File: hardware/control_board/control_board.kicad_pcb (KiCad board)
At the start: 2 copper layers, 80 x 80 mm, 125 parts, among them J1 SWD, J2 Aux, J3 Panel, J4 6.5/2mm, J5 USB_C, J6 RTD, J7 TC, J8 Conn_01x01, J9 Conn_01x01, Q1 2N7002A, Q2 IRF1018ESTRLPBF, SW1 Reset, SW2 Power, U1 STM32F103C8T6, U2 LMR38010SDDAR, U3 TLV76133DCYR, U4 USBLC6-2SC6, U5 MAX6675, U6 MCP6N11T-005E, U7 MCP6001T, U8 TLP183, Y1 8MHz

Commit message: Remove copper fills around mounting holes
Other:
- board text added: "20231127"
- board text added: "Supervisor: A. Bondyra, Ph.D."
- board text removed: "20231114"
- board text removed: "Promoter: A. Bondyra, Ph.D."

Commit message: Change MCU to STM32F103CBT6
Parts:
- U1: value STM32F103C8T6 -> STM32F103CBT6
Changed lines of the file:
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@@
         (effects (font (size 1 1) (thickness 0.15)))
     )
-    (fp_text value "STM32F103C8T6" (at 2.8 4.65) (layer "F.Fab")
+    (fp_text value "STM32F103CBT6" (at 2.8 4.65) (layer "F.Fab")
         (effects (font (size 1 1) (thickness 0.15)))
     )

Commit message: Release v1.1
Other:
- board text added: "20231129"
- board text removed: "20231127"
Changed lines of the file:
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@@
   (title_block
     (title "Reflow Hot Plate Control Board")
-    (date "2023-11-14")
+    (date "2023-11-29")
     (rev "${REVISION}")
     (company "Author: I. Kajdan")
@@
     (fp_line (start 5.625 5) (end 4.625 5)
       (stroke (width 0.1) (type solid)) (layer "F.Fab"))
-    (pad "1" smd roundrect (at -7.65 -2.54 90) (size 4.6 1.1) (layers "F.Cu" "F.Paste" "F.Mask") (roundrect_rratio 0.227273)
+    (pad "1" smd roundrect (at -7.65 -2.54 90) (size 4.6 1.1) (layers "F.Cu" "F.Paste" "F.Mask") (roundrect_rratio 0.2272727273)
       (net 24 "Net-(D9-K)") (pinfunction "G") (pintype "input"))
-    (pad "2" smd roundrect (at -0.925 -2.775 90) (size 4.55 5.25) (layers "F.Cu" "F.Paste") (roundrect_rratio 0.054945)
+    (pad "2" smd roundrect (at -0.925 -2.775 90) (size 4.55 5.25) (layers "F.Cu" "F.Paste") (roundrect_rratio 0.05494505495)
       (net 92 "Net-(D10-A)") (pinfunction "D") (pintype "passive"))
-    (pad "2" smd roundrect (at -0.925 2.775 90) (size 4.55 5.25) (layers "F.Cu" "F.Paste") (roundrect_rratio 0.054945)
+    (pad "2" smd roundrect (at -0.925 2.775 90) (size 4.55 5.25) (layers "F.Cu" "F.Paste") (roundrect_rratio 0.05494505495)
       (net 92 "Net-(D10-A)") (pinfunction "D") (pintype "passive"))
-    (pad "2" smd roundrect (at 1.5 0 90) (size 9.4 10.8) (layers "F.Cu" "F.Mask") (roundrect_rratio 0.026596)
+    (pad "2" smd roundrect (at 1.5 0 90) (size 9.4 10.8) (layers "F.Cu" "F.Mask") (roundrect_rratio 0.02659595745)
       (net 92 "Net-(D10-A)") (pinfunction "D") (pintype "passive"))
-    (pad "2" smd roundrect (at 3.925 -2.775 90) (size 4.55 5.25) (layers "F.Cu" "F.Paste") (roundrect_rratio 0.054945)
+    (pad "2" smd roundrect (at 3.925 -2.775 90) (size 4.55 5.25) (layers "F.Cu" "F.Paste") (roundrect_rratio 0.05494505495)
       (net 92 "Net-(D10-A)") (pinfunction "D") (pintype "passive"))
-    (pad "2" smd roundrect (at 3.925 2.775 90) (size 4.55 5.25) (layers "F.Cu" "F.Paste") (roundrect_rratio 0.054945)
+    (pad "2" smd roundrect (at 3.925 2.775 90) (size 4.55 5.25) (layers "F.Cu" "F.Paste") (roundrect_rratio 0.05494505495)
       (net 92 "Net-(D10-A)") (pinfunction "D") (pintype "passive"))
-    (pad "3" smd roundrect (at -7.65 2.54 90) (size 4.6 1.1) (layers "F.Cu" "F.Paste" "F.Mask") (roundrect_rratio 0.227273)
+    (pad "3" smd roundrect (at -7.65 2.54 90) (size 4.6 1.1) (layers "F.Cu" "F.Paste" "F.Mask") (roundrect_rratio 0.2272727273)
       (net 2 "GND") (pinfunction "S") (pintype "passive"))
     (model "${KICAD6_3DMODEL_DIR}/Package_TO_SOT_SMD.3dshapes/TO-263-2.wrl"
@@
     (fp_line (start 7.45 3.4) (end 7.45 -2.35)
       (stroke (width 0.1) (type solid)) (layer "F.Fab"))
-    (pad "1" thru_hole roundrect (at 0 0 90) (size 1.7 1.95) (drill 0.95) (layers "*.Cu" "*.Mask") (roundrect_rratio 0.147059)
+    (pad "1" thru_hole roundrect (at 0 0 90) (size 1.7 1.95) (drill 0.95) (layers "*.Cu" "*.Mask") (roundrect_rratio 0.1470588235)
       (net 50 "/Temperature Sensors/IN+") (pinfunction "Pin_1") (pintype "passive"))
     (pad "2" thru_hole oval (at 2.5 0 90) (size 1.7 1.95) (drill 0.95) (layers "*.Cu" "*.Mask")
@@
     (fp_line (start 4.95 3.4) (end 4.95 -2.35)
       (stroke (width 0.1) (type solid)) (layer "F.Fab"))
-    (pad "1" thru_hole roundrect (at 0 0 90) (size 1.7 2) (drill 1) (layers "*.Cu" "*.Mask") (roundrect_rratio 0.147059)
+    (pad "1" thru_hole roundrect (at 0 0 90) (size 1.7 2) (drill 1) (layers "*.Cu" "*.Mask") (roundrect_rratio 0.1470588235)
       (net 84 "Net-(J7-Pin_1)") (pinfunction "Pin_1") (pintype "passive"))
     (pad "2" thru_hole oval (at 2.5 0 90) (size 1.7 2) (drill 1) (layers "*.Cu" "*.Mask")
@@
     (fp_line (start 2.25 1.6) (end -2.25 1.6)
       (stroke (width 0.1) (type solid)) (layer "F.Fab"))
-    (pad "1" smd roundrect (at -2.1375 0) (size 1.125 3.4) (layers "F.Cu" "F.Paste" "F.Mask") (roundrect_rratio 0.222222)
+    (pad "1" smd roundrect (at -2.1375 0) (size 1.125 3.4) (layers "F.Cu" "F.Paste" "F.Mask") (roundrect_rratio 0.2222222222)
       (net 23 "+24V") (pintype "passive"))
-    (pad "2" smd roundrect (at 2.1375 0) (size 1.125 3.4) (layers "F.Cu" "F.Paste" "F.Mask") (roundrect_rratio 0.222222)
+    (pad "2" smd roundrect (at 2.1375 0) (size 1.125 3.4) (layers "F.Cu" "F.Paste" "F.Mask") (roundrect_rratio 0.2222222222)
       (net 7 "/Power Supply/VIN") (pintype "passive"))
     (model "${KICAD6_3DMODEL_DIR}/Fuse.3dshapes/Fuse_1206_3216Metric.wrl"
@@
   (gr_line locked (start 176 120.5) (end 176 79.5)
     (stroke (width 0.1) (type default)) (layer "Edge.Cuts"))
-  (gr_text "20231127" (at 164 71.35) (layer "B.SilkS")
+  (gr_text "20231129" (at 164 71.35) (layer "B.SilkS")
     (effects (font (size 1 1) (thickness 0.15)) (justify mirror))
   )

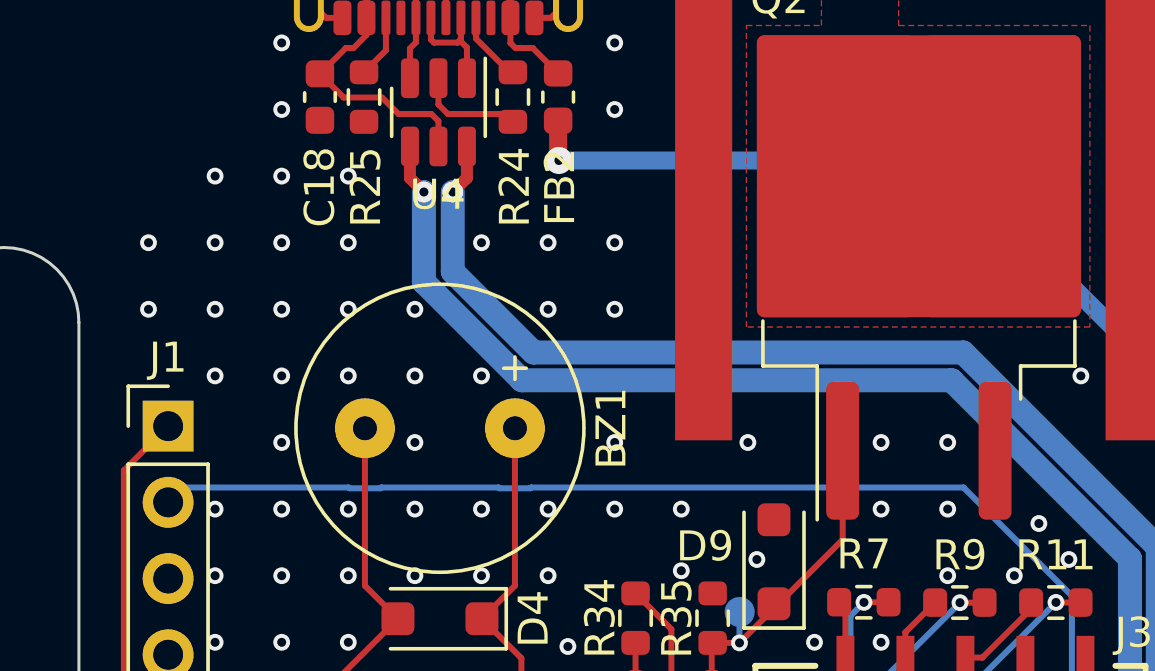
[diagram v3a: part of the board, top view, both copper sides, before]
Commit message: Remove the JLC placeholder
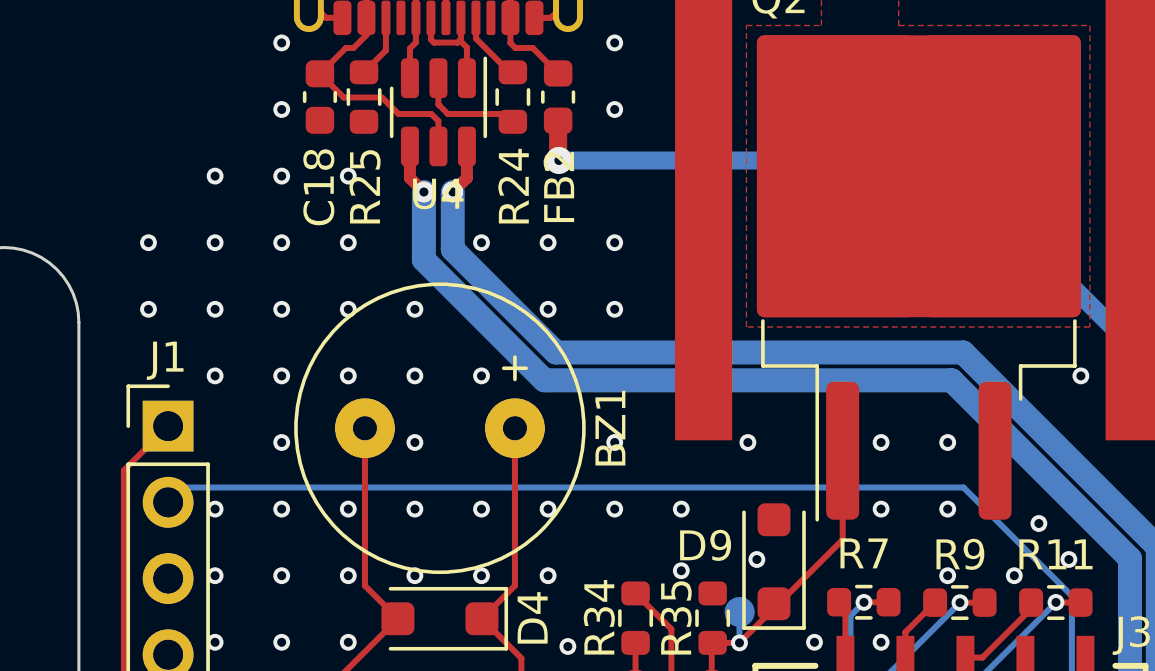
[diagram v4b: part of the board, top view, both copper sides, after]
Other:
- board text added: "20231130"
- board text removed: "20231129"
- board text removed: "JLCJLCJLCJLC"
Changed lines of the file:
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@@
   (title_block
     (title "Reflow Hot Plate Control Board")
-    (date "2023-11-29")
+    (date "2023-11-30")
     (rev "${REVISION}")
     (company "Author: I. Kajdan")
@@
     (property "ki_description" "Single Pole Single Throw (SPST) switch")
     (property "ki_keywords" "switch lever")
-    (attr exclude_from_pos_files)
+    (attr exclude_from_pos_files exclude_from_bom)
     (fp_text reference "SW2" (at 2.25 2.2 -180) (layer "F.SilkS")
         (effects (font (size 1 1) (thickness 0.15)))
@@
   (gr_line locked (start 176 120.5) (end 176 79.5)
     (stroke (width 0.1) (type default)) (layer "Edge.Cuts"))
-  (gr_text "20231129" (at 164 71.35) (layer "B.SilkS")
+  (gr_text "20231130" (at 164 71.35) (layer "B.SilkS")
     (effects (font (size 1 1) (thickness 0.15)) (justify mirror))
   )
@@
     (effects (font (size 1 1) (thickness 0.15)) (justify mirror))
   )
-  (gr_text "JLCJLCJLCJLC" (at 148 135.6) (layer "B.SilkS")
-    (effects (font (size 1 1) (thickness 0.15)) (justify mirror))
-  )
   (gr_text "Author:\nI. Kajdan" (at 174.35 120.65) (layer "B.SilkS")
     (effects (font (size 1 1) (thickness 0.15)) (justify left mirror))
@@
   (segment (start 150.75 99.75) (end 150.75 100.3375) (width 0.2) (layer "F.Cu") (net 28))
   (via (at 151.620585 99.396424) (size 0.56) (drill 0.3) (layers "F.Cu" "B.Cu") (net 28))
+  (segment (start 153.1 97.917009) (end 153.1 88.610966) (width 0.2) (layer "B.Cu") (net 28))
   (segment (start 151.620585 99.396424) (end 153.1 97.917009) (width 0.2) (layer "B.Cu") (net 28))
   (segment (start 123.47 85) (end 122.975 85.495) (width 0.2) (layer "B.Cu") (net 28))
-  (segment (start 149.489034 85) (end 135.077767 85) (width 0.2) (layer "B.Cu") (net 28))
-  (segment (start 134.017233 85.025) (end 133.992233 85) (width 0.2) (layer "B.Cu") (net 28))
-  (segment (start 129.017233 85.025) (end 128.992233 85) (width 0.2) (layer "B.Cu") (net 28))
   (segment (start 153.1 88.610966) (end 149.489034 85) (width 0.2) (layer "B.Cu") (net 28))
-  (segment (start 128.992233 85) (end 123.47 85) (width 0.2) (layer "B.Cu") (net 28))
-  (segment (start 135.052767 85.025) (end 134.017233 85.025) (width 0.2) (layer "B.Cu") (net 28))
-  (segment (start 130.077767 85) (end 130.052767 85.025) (width 0.2) (layer "B.Cu") (net 28))
-  (segment (start 133.992233 85) (end 130.077767 85) (width 0.2) (layer "B.Cu") (net 28))
-  (segment (start 153.1 97.917009) (end 153.1 88.610966) (width 0.2) (layer "B.Cu") (net 28))
-  (segment (start 130.052767 85.025) (end 129.017233 85.025) (width 0.2) (layer "B.Cu") (net 28))
-  (segment (start 135.077767 85) (end 135.052767 85.025) (width 0.2) (layer "B.Cu") (net 28))
+  (segment (start 149.489034 85) (end 123.47 85) (width 0.2) (layer "B.Cu") (net 28))
   (segment (start 150.75 102) (end 150.75 102.034619) (width 0.2) (layer "F.Cu") (net 29))
   (segment (start 134.826052 102.325586) (end 132.9 100.399534) (width 0.2) (layer "F.Cu") (net 29))
@@
   (via (at 132.4635 75.15) (size 0.7) (drill 0.3) (layers "F.Cu" "B.Cu") (net 76))
   (via (at 150.9 103.9635) (size 0.7) (drill 0.3) (layers "F.Cu" "B.Cu") (net 76))
-  (segment (start 155.9635 99.691988) (end 155.9635 86.98857) (width 0.8) (layer "B.Cu") (net 76))
-  (segment (start 149.47493 80.5) (end 135.155488 80.5) (width 0.8) (layer "B.Cu") (net 76))
-  (segment (start 132.4635 77.808012) (end 132.4635 75.15) (width 0.8) (layer "B.Cu") (net 76))
+  (segment (start 135.9 80.5) (end 132.4635 77.0635) (width 0.8) (layer "B.Cu") (net 76))
   (segment (start 150.9 103.9635) (end 151.691988 103.9635) (width 0.8) (layer "B.Cu") (net 76))
-  (segment (start 155.9635 86.98857) (end 149.47493 80.5) (width 0.8) (layer "B.Cu") (net 76))
+  (segment (start 132.4635 77.0635) (end 132.4635 75.15) (width 0.8) (layer "B.Cu") (net 76))
   (segment (start 151.691988 103.9635) (end 155.9635 99.691988) (width 0.8) (layer "B.Cu") (net 76))
-  (segment (start 135.155488 80.5) (end 132.4635 77.808012) (width 0.8) (layer "B.Cu") (net 76))
+  (segment (start 155.9635 86.98857) (end 149.47493 80.5) (width 0.8) (layer "B.Cu") (net 76))
+  (segment (start 149.47493 80.5) (end 135.9 80.5) (width 0.8) (layer "B.Cu") (net 76))
+  (segment (start 155.9635 99.691988) (end 155.9635 86.98857) (width 0.8) (layer "B.Cu") (net 76))
   (segment (start 152.1625 103.25) (end 151.1135 103.25) (width 0.2) (layer "F.Cu") (net 77))
   (segment (start 153.34 103.25) (end 153.855 103.765) (width 0.2) (layer "F.Cu") (net 77))
@@
   (via (at 131.5 75.15) (size 0.7) (drill 0.3) (layers "F.Cu" "B.Cu") (net 77))
   (via (at 150.9 103.0365) (size 0.7) (drill 0.3) (layers "F.Cu" "B.Cu") (net 77))
-  (segment (start 155.0365 87.372546) (end 155.0365 99.308012) (width 0.8) (layer "B.Cu") (net 77))
-  (segment (start 131.5 78.155488) (end 134.771512 81.427) (width 0.8) (layer "B.Cu") (net 77))
-  (segment (start 151.308012 103.0365) (end 150.9 103.0365) (width 0.8) (layer "B.Cu") (net 77))
+  (segment (start 135.516024 81.427) (end 149.090954 81.427) (width 0.8) (layer "B.Cu") (net 77))
+  (segment (start 131.5 75.15) (end 131.5 77.410976) (width 0.8) (layer "B.Cu") (net 77))
   (segment (start 155.0365 99.308012) (end 151.308012 103.0365) (width 0.8) (layer "B.Cu") (net 77))
+  (segment (start 151.308012 103.0365) (end 150.9 103.0365) (width 0.8) (layer "B.Cu") (net 77))
+  (segment (start 131.5 77.410976) (end 135.516024 81.427) (width 0.8) (layer "B.Cu") (net 77))
+  (segment (start 155.0365 87.372546) (end 155.0365 99.308012) (width 0.8) (layer "B.Cu") (net 77))
   (segment (start 149.090954 81.427) (end 155.0365 87.372546) (width 0.8) (layer "B.Cu") (net 77))
-  (segment (start 134.771512 81.427) (end 149.090954 81.427) (width 0.8) (layer "B.Cu") (net 77))
-  (segment (start 131.5 75.15) (end 131.5 78.155488) (width 0.8) (layer "B.Cu") (net 77))
   (segment (start 130.235 69.345) (end 130.235 70.43) (width 0.2) (layer "F.Cu") (net 78))
   (segment (start 130.235 70.43) (end 129.505 71.16) (width 0.2) (layer "F.Cu") (net 78))

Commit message: Swap the left and right button signals
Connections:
- R10 pad 1: /BUTTON_RIGHT -> /BUTTON_LEFT
- R9 pad 1: /BUTTON_LEFT -> /BUTTON_RIGHT
- U1 pad 45: /BUTTON_RIGHT -> /BUTTON_LEFT
- U1 pad 46: /BUTTON_LEFT -> /BUTTON_RIGHT
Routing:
- net /BUTTON_RIGHT: track 1.76 -> 15.9 mm, vias 0 -> 2
- net /BUTTON_LEFT: track 15.9 -> 1.76 mm, vias 2 -> 0
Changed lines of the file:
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@@
       (stroke (width 0.1) (type solid)) (layer "F.Fab"))
     (pad "1" smd roundrect (at -0.825 0 180) (size 0.8 0.95) (layers "F.Cu" "F.Paste" "F.Mask") (roundrect_rratio 0.25)
-      (net 36 "/BUTTON_LEFT") (pintype "passive"))
+      (net 37 "/BUTTON_RIGHT") (pintype "passive"))
     (pad "2" smd roundrect (at 0.825 0 180) (size 0.8 0.95) (layers "F.Cu" "F.Paste" "F.Mask") (roundrect_rratio 0.25)
       (net 52 "Net-(J3-Pin_7)") (pintype "passive"))
@@
     (property "Sheetfile" "power_supply.kicad_sch")
     (property "Sheetname" "Power Supply")
+    (property "exclude_from_bom" "")
     (property "ki_description" "Single Pole Single Throw (SPST) switch")
     (property "ki_keywords" "switch lever")
@@
       (stroke (width 0.1) (type solid)) (layer "F.Fab"))
     (pad "1" smd roundrect (at -0.825 0 90) (size 0.8 0.95) (layers "F.Cu" "F.Paste" "F.Mask") (roundrect_rratio 0.25)
-      (net 37 "/BUTTON_RIGHT") (pintype "passive"))
+      (net 36 "/BUTTON_LEFT") (pintype "passive"))
     (pad "2" smd roundrect (at 0.825 0 90) (size 0.8 0.95) (layers "F.Cu" "F.Paste" "F.Mask") (roundrect_rratio 0.25)
       (net 51 "Net-(J3-Pin_6)") (pintype "passive"))
@@
       (net 55 "Net-(U1-BOOT0)") (pinfunction "BOOT0") (pintype "input"))
     (pad "45" smd roundrect (at -1.25 -4.1625) (size 0.3 1.475) (layers "F.Cu" "F.Paste" "F.Mask") (roundrect_rratio 0.25)
-      (net 37 "/BUTTON_RIGHT") (pinfunction "PB8") (pintype "bidirectional"))
+      (net 36 "/BUTTON_LEFT") (pinfunction "PB8") (pintype "bidirectional"))
     (pad "46" smd roundrect (at -1.75 -4.1625) (size 0.3 1.475) (layers "F.Cu" "F.Paste" "F.Mask") (roundrect_rratio 0.25)
-      (net 36 "/BUTTON_LEFT") (pinfunction "PB9") (pintype "bidirectional"))
+      (net 37 "/BUTTON_RIGHT") (pinfunction "PB9") (pintype "bidirectional"))
     (pad "47" smd roundrect (at -2.25 -4.1625) (size 0.3 1.475) (layers "F.Cu" "F.Paste" "F.Mask") (roundrect_rratio 0.25)
       (net 2 "GND") (pinfunction "VSS") (pintype "passive"))
@@
   (segment (start 145.72 101.78) (end 145.72 89.2795) (width 0.2) (layer "B.Cu") (net 35))
   (segment (start 145.225 102.275) (end 145.72 101.78) (width 0.2) (layer "B.Cu") (net 35))
-  (segment (start 149.3695 88.84) (end 150.185 88.84) (width 0.2) (layer "F.Cu") (net 36))
-  (segment (start 150.185 88.84) (end 150.19 88.835) (width 0.2) (layer "F.Cu") (net 36))
-  (segment (start 146.25 100.3375) (end 146.25 101.5) (width 0.2) (layer "F.Cu") (net 36))
-  (via (at 149.3695 88.84) (size 0.56) (drill 0.3) (layers "F.Cu" "B.Cu") (net 36))
-  (via (at 146.25 101.5) (size 0.56) (drill 0.3) (layers "F.Cu" "B.Cu") (net 36))
-  (segment (start 146.25 91.9595) (end 149.3695 88.84) (width 0.2) (layer "B.Cu") (net 36))
-  (segment (start 146.25 101.5) (end 146.25 91.9595) (width 0.2) (layer "B.Cu") (net 36))
-  (segment (start 146.465 98.695) (end 146.75 98.98) (width 0.2) (layer "F.Cu") (net 37))
-  (segment (start 146.75 98.98) (end 146.75 100.3375) (width 0.2) (layer "F.Cu") (net 37))
+  (segment (start 146.465 98.695) (end 146.75 98.98) (width 0.2) (layer "F.Cu") (net 36))
+  (segment (start 146.75 98.98) (end 146.75 100.3375) (width 0.2) (layer "F.Cu") (net 36))
+  (segment (start 149.3695 88.84) (end 150.185 88.84) (width 0.2) (layer "F.Cu") (net 37))
+  (segment (start 150.185 88.84) (end 150.19 88.835) (width 0.2) (layer "F.Cu") (net 37))
+  (segment (start 146.25 100.3375) (end 146.25 101.5) (width 0.2) (layer "F.Cu") (net 37))
+  (via (at 149.3695 88.84) (size 0.56) (drill 0.3) (layers "F.Cu" "B.Cu") (net 37))
+  (via (at 146.25 101.5) (size 0.56) (drill 0.3) (layers "F.Cu" "B.Cu") (net 37))
+  (segment (start 146.25 91.9595) (end 149.3695 88.84) (width 0.2) (layer "B.Cu") (net 37))
+  (segment (start 146.25 101.5) (end 146.25 91.9595) (width 0.2) (layer "B.Cu") (net 37))
   (segment (start 159.685 120.3) (end 156.46 120.3) (width 0.2) (layer "F.Cu") (net 38))
   (segment (start 149.25 110.035) (end 149.25 108.6625) (width 0.2) (layer "F.Cu") (net 38))
